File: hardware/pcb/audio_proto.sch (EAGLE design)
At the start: 23 parts, among them IC1 MCP1700

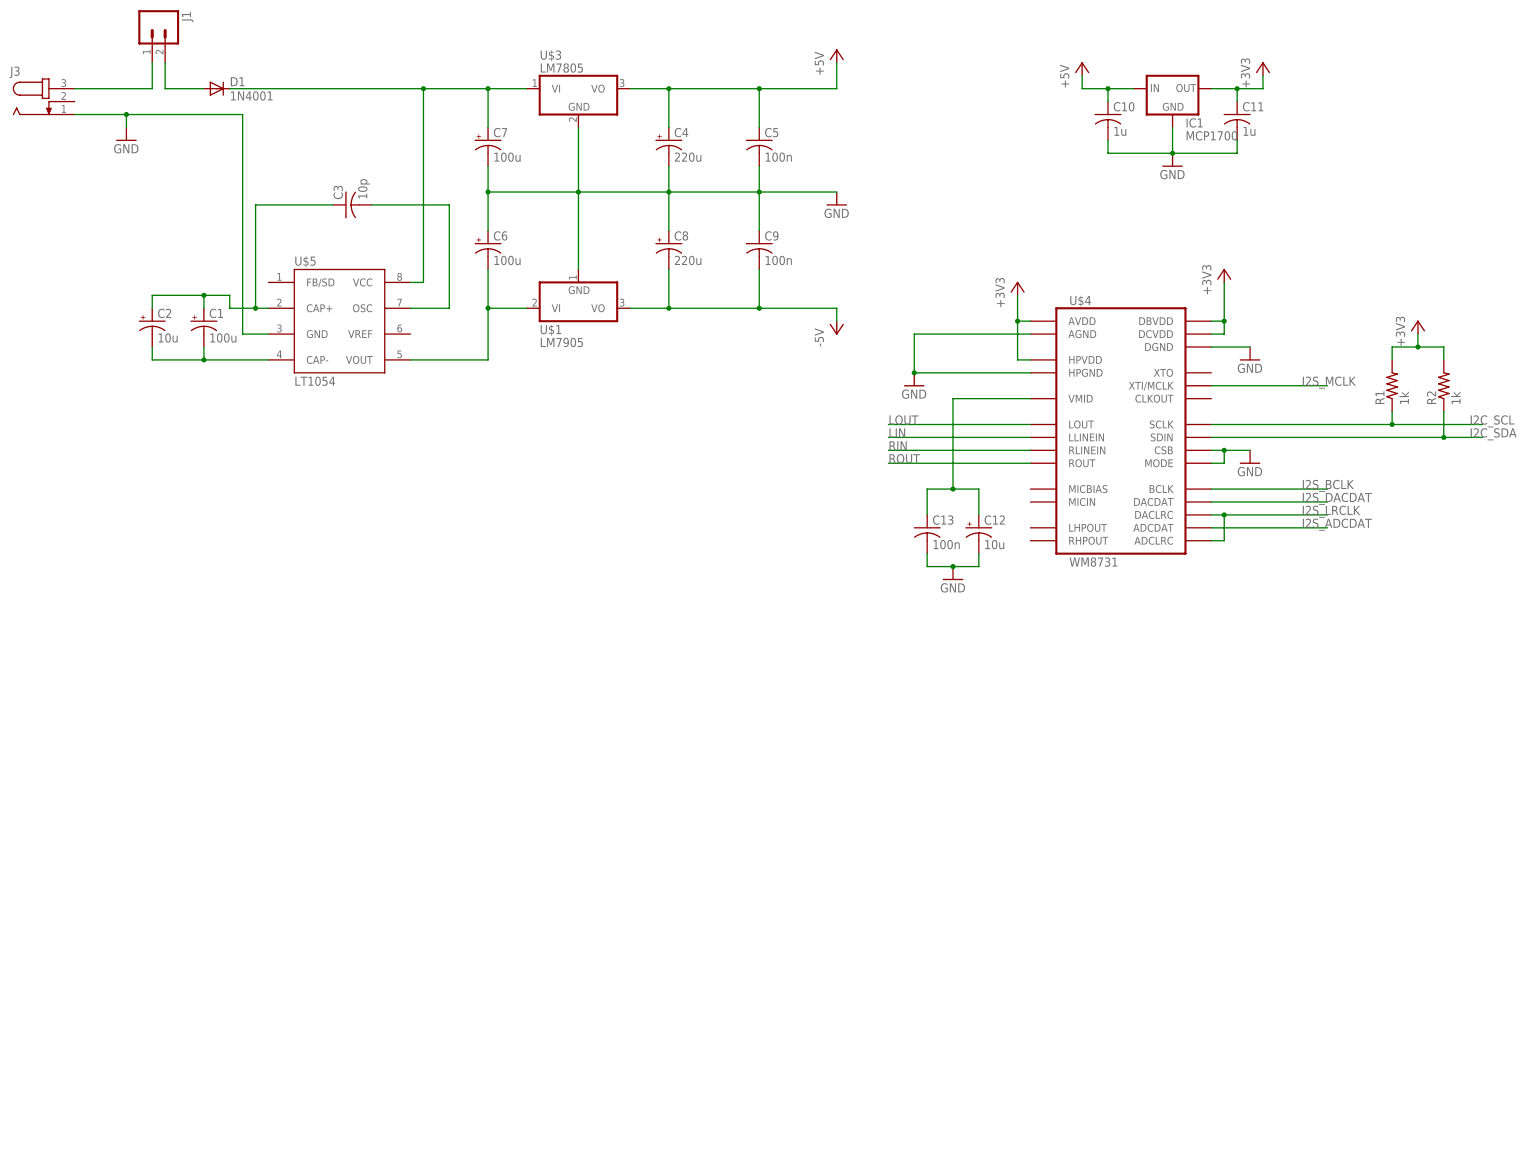
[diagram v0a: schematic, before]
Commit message: Added audio IO, updated lbr.
Signed-off-by: Theo Zanellato <theo.zanellato@gmail.com>
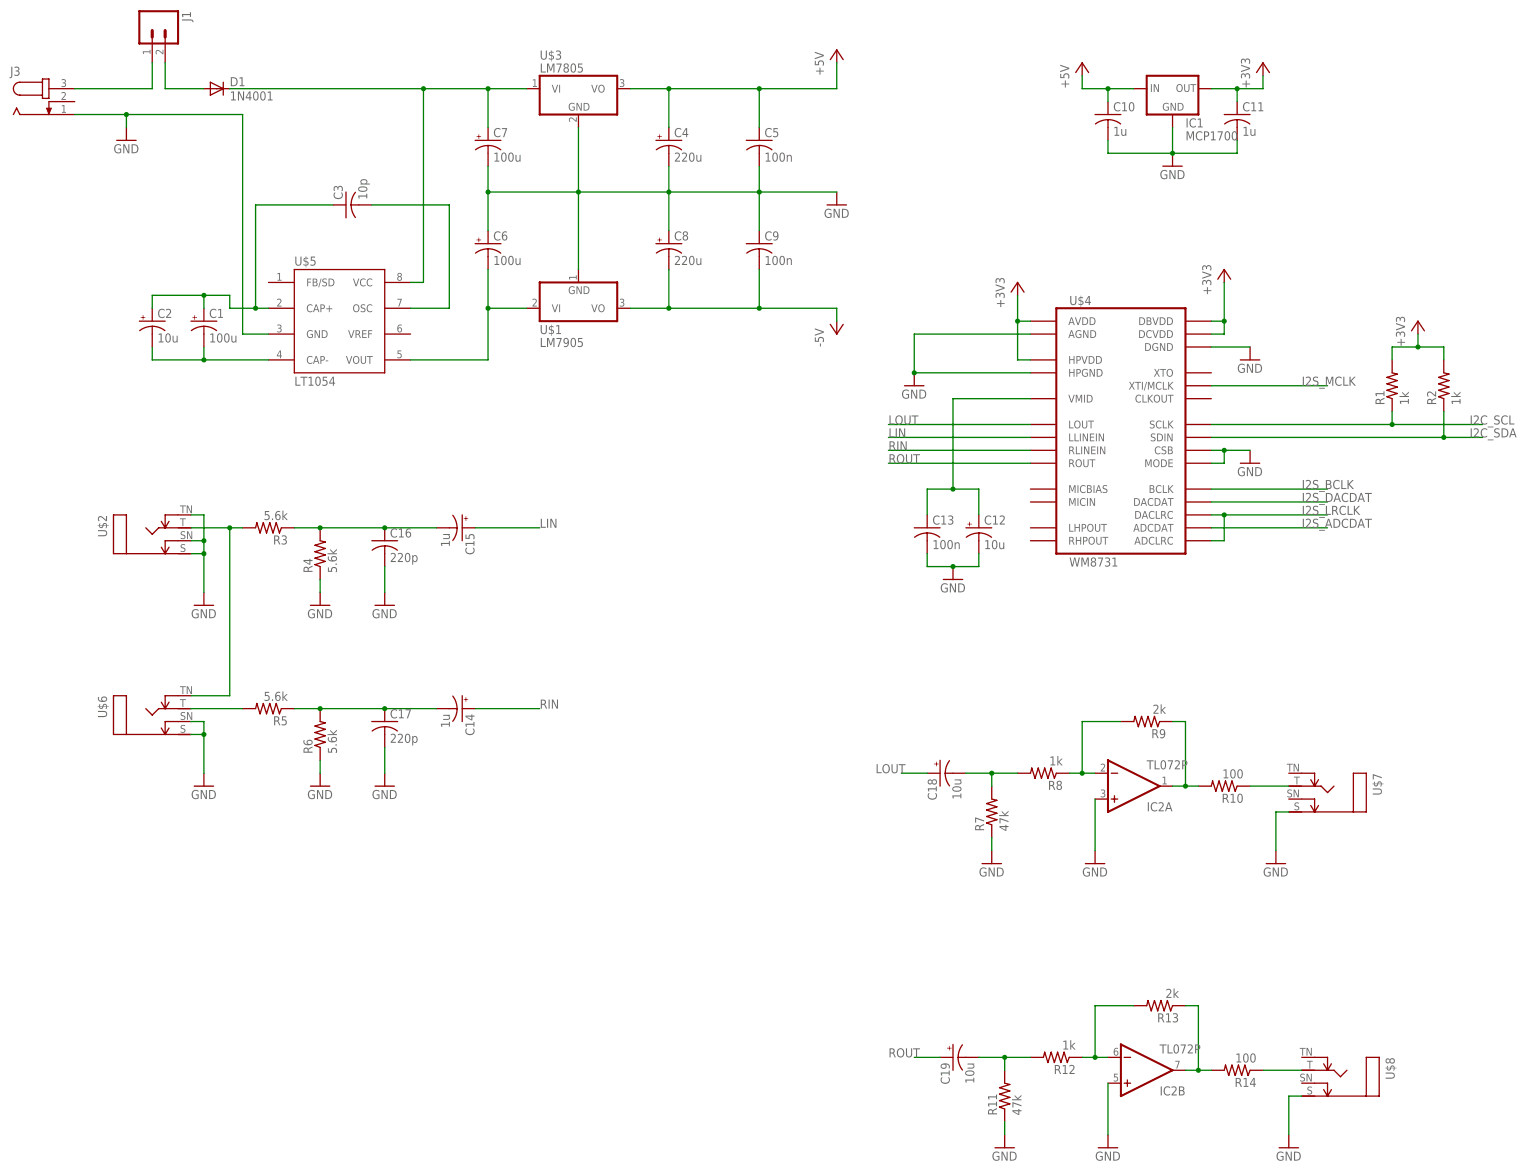
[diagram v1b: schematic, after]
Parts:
- added C14, C15: 1u, rcl:CPOL-USE2.5-6
- added C16, C17: 220p, rcl:C-US025-025X050
- added C18, C19: 10u, rcl:CPOL-USE2.5-6
- added IC2: TL072P, linear:TL072P
- added R10, R14: 100, rcl:R-US_0207/10
- added R11, R7: 47k, rcl:R-US_0207/10
- added R12, R8: 1k, rcl:R-US_0207/10
- added R13, R9: 2k, rcl:R-US_0207/10
- added R3, R4, R5, R6: 5.6k, rcl:R-US_0207/10
- added U$2, U$6, U$7, U$8: MONOJACKSW, mankell-proto:MONOJACKSW
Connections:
- new net N$11: R5.2, U$6.T
- new net N$12: C14.-, C17.1, R5.1, R6.2
- new net N$13: C18.-, R7.2, R8.2
- new net N$14: IC2A.-IN, R8.1, R9.2
- new net N$15: IC2A.OUT, R10.2, R9.1
- new net N$16: R10.1, U$7.T
- new net N$17: C19.-, R11.2, R12.2
- new net N$18: IC2B.-IN, R12.1, R13.2
- new net N$19: IC2B.OUT, R13.1, R14.2
- new net N$20: R14.1, U$8.T
- new net N$3: R3.2, U$2.T, U$6.TN
- new net N$8: C15.-, C16.1, R3.1, R4.2
- net GND: now also C16.2, C17.2, IC2A.+IN, IC2B.+IN, R11.1, R4.1, R6.1, R7.1, U$2.S, U$2.SN, U$2.TN, U$6.S, U$6.SN, U$7.S, U$8.S
- net LIN: now also C15.+
- net LOUT: now also C18.+
- net RIN: now also C14.+
- net ROUT: now also C19.+
